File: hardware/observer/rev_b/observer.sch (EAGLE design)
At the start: 54 parts, among them J1 CON_HEADER_2X05-SMD+SHROUDED, J2 CON_HEADER_2X05-SMD+SHROUDED, J3 TC2030-CC2538-BL-NL, J4 JUMPER-PTH-2-NO, J5 PINHD-2X8/SMD, J6 CON_HEADER_2X05-PTH+SHROUDED_A, P9/P8 BBB_HEADER, U1 LPS331AP, U2 MPU-9250, U3 SI1147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

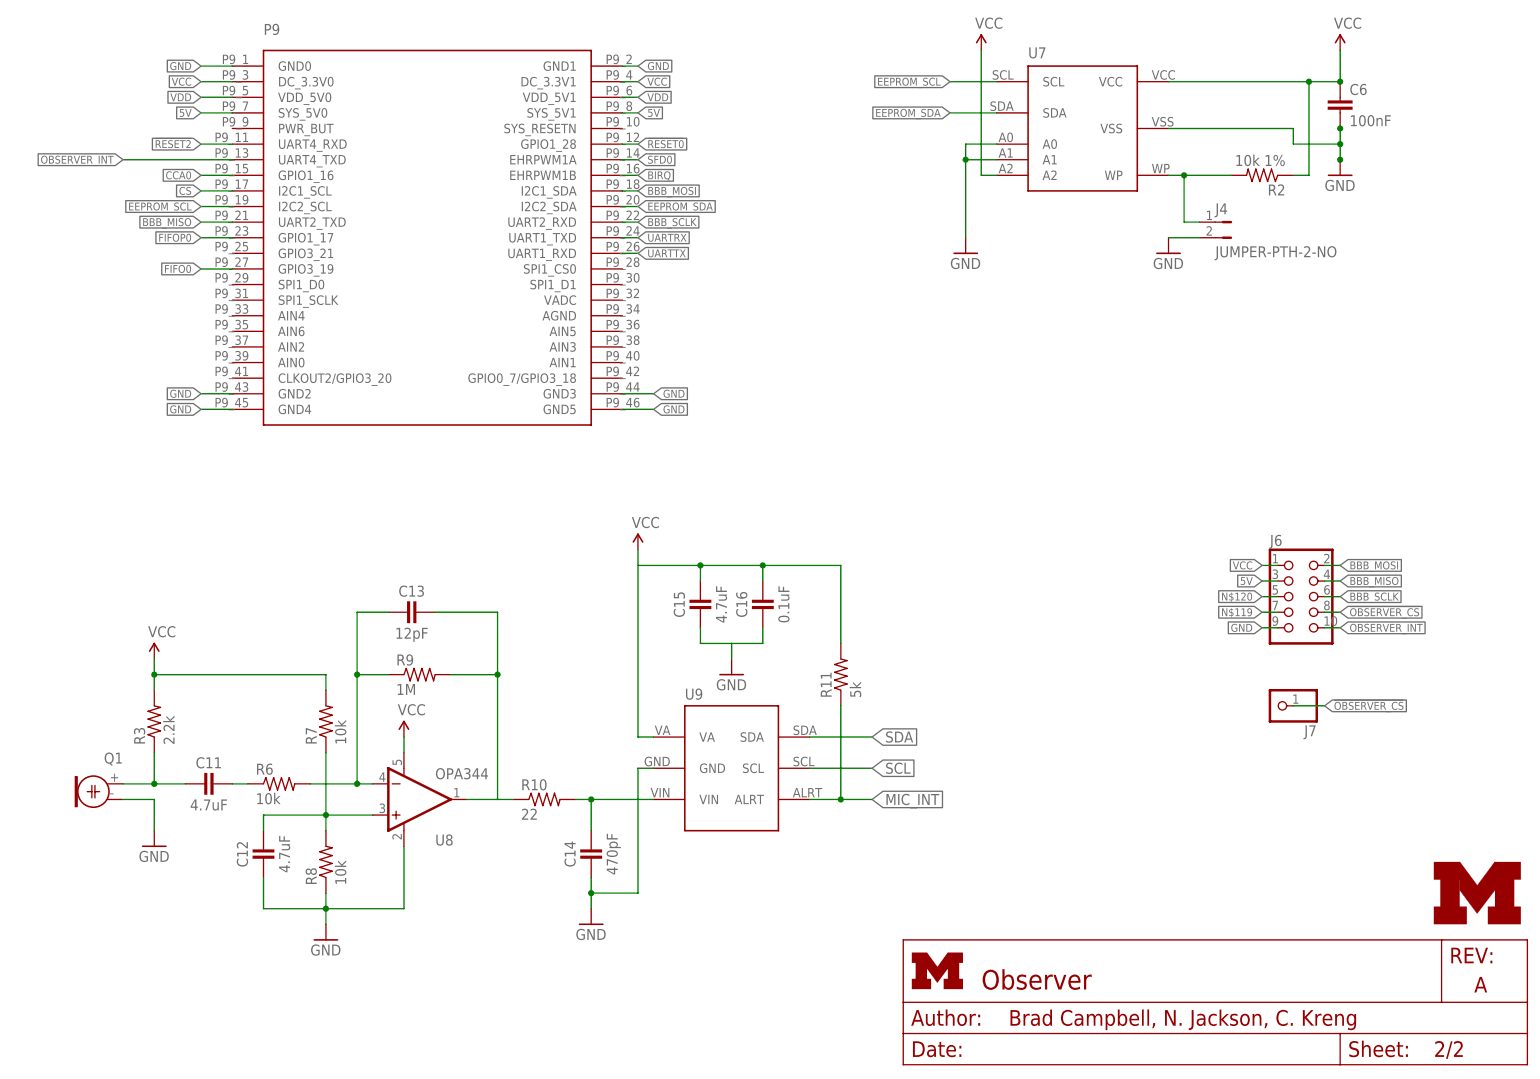
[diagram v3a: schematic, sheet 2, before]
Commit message: Fixed header on motherboard, added decoupling cap for op amp
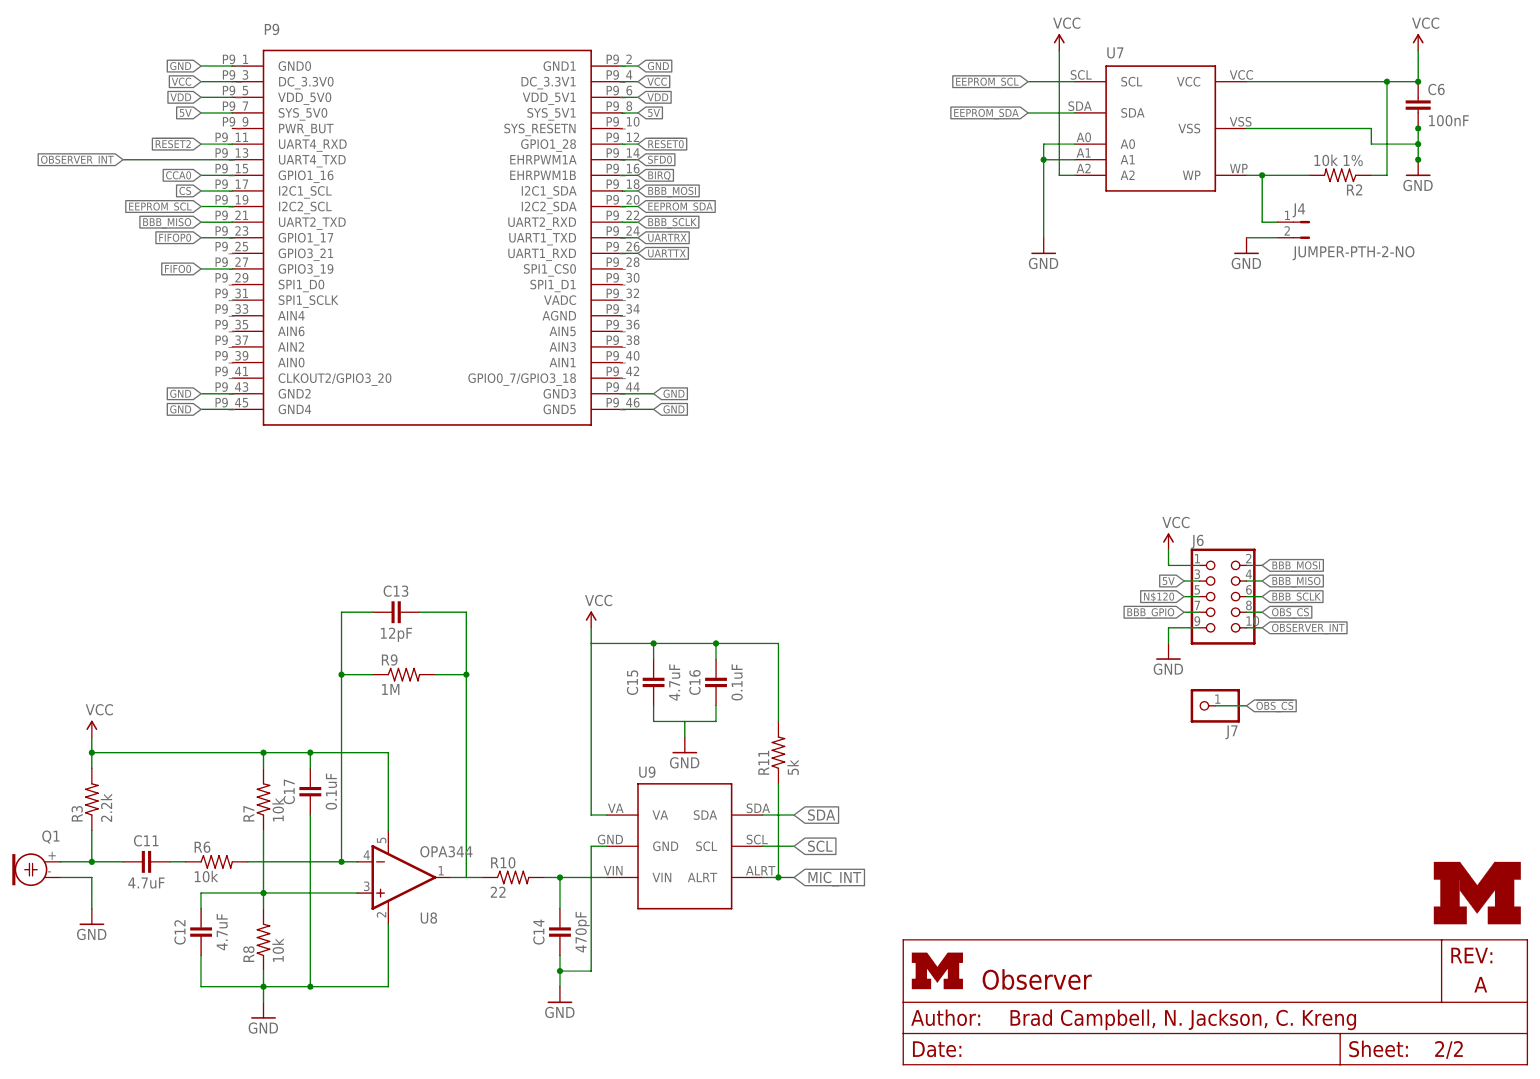
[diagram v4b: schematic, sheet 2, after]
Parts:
- added C17: 0.1uF, passives:CAPACITOR
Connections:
- net !OBSERVER_CS renamed !OBS_CS
- removed net N$119: J6.7
- net BBB_GPIO: now also J6.7
- net GND: now also C17.2
- net N$9: now also C13.2
- net VCC: now also C17.1
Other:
- note added: "Microphone, ADC"
- moved on the sheet: C11, C12, C13, C14, C15, C16, C6, J4, J6, J7, Q1, R10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

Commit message: Renamed passives in order of increasing value, highlighted parts needed in bom
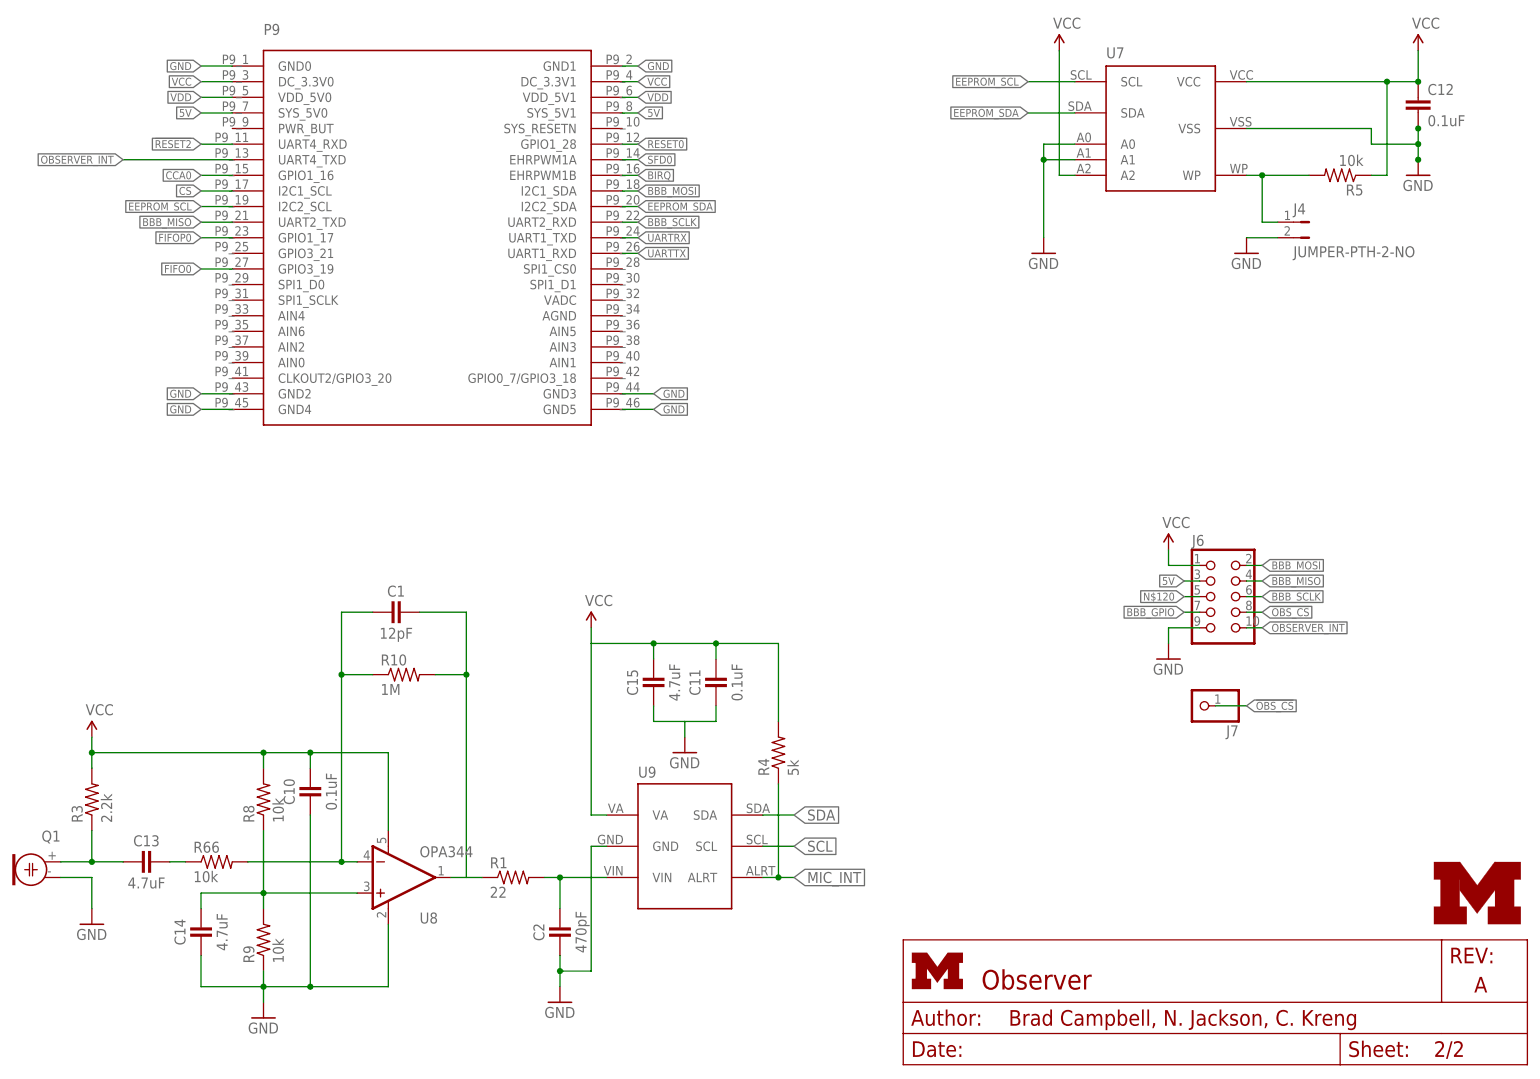
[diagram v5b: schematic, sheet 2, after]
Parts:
- removed R11: 5k, passives:RESISTOR0402_RES
- added R66: 10k, passives:RESISTOR0402_RES
- C1: value 10nF -> 12pF; DIGIKEY 490-1312-1-ND -> (none)
- C10: value 22uF -> 0.1uF; device passives:CAP_POL0603 -> passives:CAPACITOR; DIGIKEY 511-1493-1-ND -> (none)
- C11: value 4.7uF -> 0.1uF
- C12: value 4.7uF -> 0.1uF; device passives:CAPACITOR -> rcl:C-EUC0402; DIGIKEY (none) -> 490-1318-1-ND
- C13: value 12pF -> 4.7uF
- C14: value 470pF -> 4.7uF
- C16: value 0.1uF -> 10uF; DIGIKEY (none) -> 445-8919-1-ND
- C17: value 0.1uF -> 22uF; device passives:CAPACITOR -> passives:CAP_POL0603; DIGIKEY (none) -> 511-1493-1-ND
- C2: value 0.1uF -> 470pF; DIGIKEY 490-1318-1-ND -> (none)
- C3: value 0.1uF -> 10nF; DIGIKEY 490-1318-1-ND -> 490-1312-1-ND
- C6: value 100nF -> 0.1uF; device rcl:C-EUC0402 -> passives:CAPACITOR
- C9: value 10uF -> 0.1uF; DIGIKEY 445-8919-1-ND -> 490-1318-1-ND
- R1: value 30 -> 22; DIGIKEY RHM30CECT-ND -> (none)
- R10: value 22 -> 1M
- R2: value 10k 1% -> 30; device rcl:R-US_R0402 -> passives:RESISTOR0402_RES; DIGIKEY RHM1.00MCDCT-ND -> RHM30CECT-ND
- R4: value 10k -> 5k; DIGIKEY RHM10.0KCDCT-ND -> (none)
- R5: device passives:RESISTOR0402_RES -> rcl:R-US_R0402; DIGIKEY RHM10.0KCDCT-ND -> RHM1.00MCDCT-ND
- R6, R7: DIGIKEY (none) -> RHM10.0KCDCT-ND
- R9: value 1M -> 10k
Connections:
- net GND: now also C10.2, C11.2, C17.ANODE, R9.1; no longer C1.2, C10.ANODE, C17.2, R8.1
- net MIC_AIN: now also C1.1, R1.1, R10.2; no longer C13.1, R10.1, R9.2
- net MIC_INT: now also R4.1; no longer R11.1
- net N$1: now also C13.2; no longer C11.2
- net N$10: now also C14.1, R8.1, R9.2; no longer C12.1, R7.1, R8.2
- net N$11: now also C2.1, R1.2; no longer C14.1, R10.2
- net N$31: now also R5.2; no longer R2.2
- net N$5: now also C13.1, R66.1; no longer C11.1, R6.1
- net N$8: now also C17.CATHODE, R2.1; no longer C10.CATHODE, R1.1
- net N$9: now also C1.2, R10.1, R66.2; no longer C13.2, R6.2, R9.1
- net SCL: now also R7.1; no longer R5.1
- net SDA: now also R6.1; no longer R4.1
- net VCC: now also C10.1, C11.1, C12.1, R2.2, R5.1, R6.2, R8.2; no longer C1.1, C17.1, C2.1, R1.2, R11.2, R2.1, R5.2
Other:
- moved on the sheet: C11, C13, C14, C3, C7, C9, R10, R8, R9

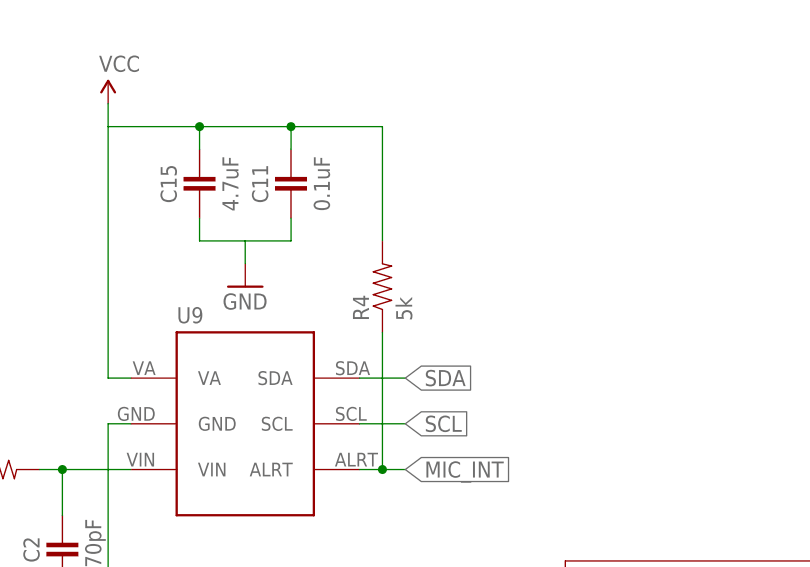
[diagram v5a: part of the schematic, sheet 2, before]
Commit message: Shipped off board, fixed DRU errors.
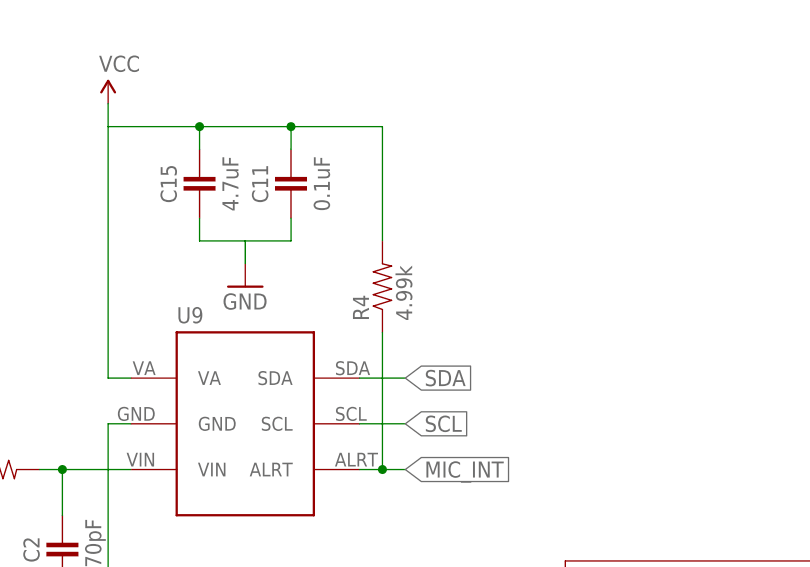
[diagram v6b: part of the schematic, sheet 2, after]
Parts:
- R4: value 5k -> 4.99k
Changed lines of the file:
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@@
 <part name="C15" library="passives" deviceset="CAPACITOR" device="" value="4.7uF"/>
 <part name="C11" library="passives" deviceset="CAPACITOR" device="" value="0.1uF"/>
-<part name="R4" library="passives" deviceset="RESISTOR" device="0402_RES" value="5k"/>
+<part name="R4" library="passives" deviceset="RESISTOR" device="0402_RES" value="4.99k"/>
 <part name="GND26" library="SparkFun-Aesthetics" deviceset="GND" device=""/>
 <part name="GND27" library="SparkFun-Aesthetics" deviceset="GND" device=""/>
